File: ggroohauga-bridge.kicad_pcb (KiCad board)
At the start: 2 copper layers, 101.6 x 31 mm, 6 parts

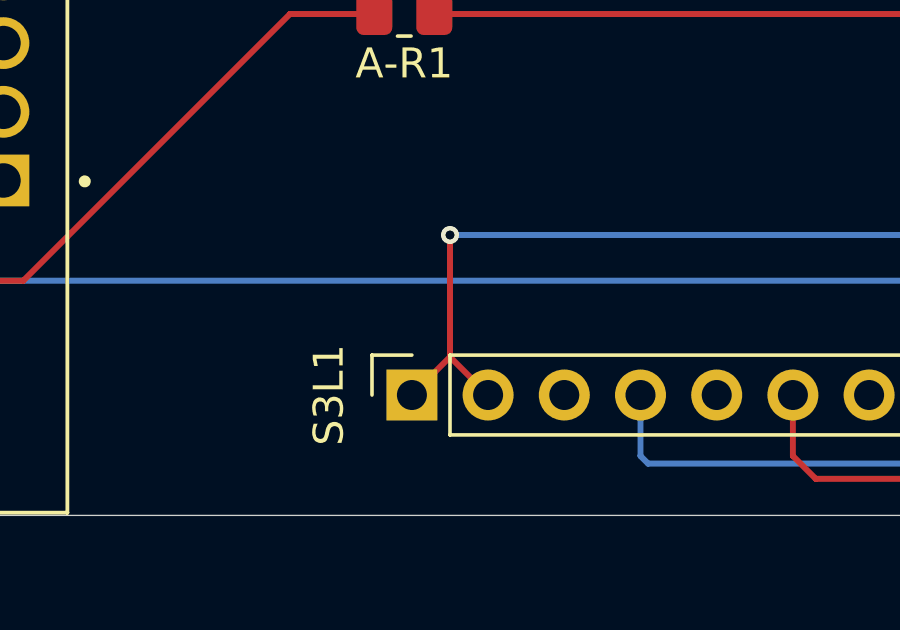
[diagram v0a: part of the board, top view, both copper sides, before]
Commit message: Fix compatibility with ESP32-S3-DevKitM-1
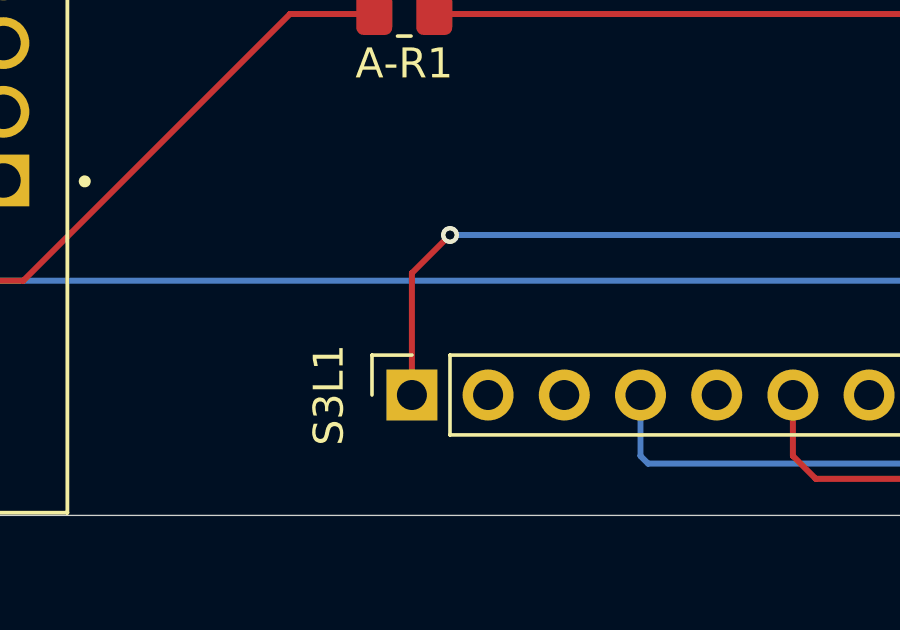
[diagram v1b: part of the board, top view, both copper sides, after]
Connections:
- S3L1 pad 2: +3.3V -> unconnected-(S3L1-Pin_2-Pad2)
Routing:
- net +3.3V: track 59.6 -> 57.8 mm
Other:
- board text added: "urn:oid:1.3.6.1.4.1.39777.1.3.1.3.1 https://github.com/nomis/ggroohauga-pcb (bridge)"
- board text removed: "urn:oid:1.3.6.1.4.1.39777.1.3.1.3.0 https://github.com/nomis/ggroohauga-pcb (bridge)"
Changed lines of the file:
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@@
 	(net 58 "unconnected-(C-J1-Pad3)")
 	(net 59 "unconnected-(C-J1-Pad4)")
+	(net 60 "unconnected-(S3L1-Pin_2-Pad2)")
 	(footprint "Connector_PinSocket_2.54mm:PinSocket_1x20_P2.54mm_Vertical"
 		(layer "F.Cu")
@@
 			)
 			(remove_unused_layers no)
-			(net 21 "+3.3V")
+			(net 60 "unconnected-(S3L1-Pin_2-Pad2)")
 			(pinfunction "Pin_2")
-			(pintype "passive")
+			(pintype "passive+no_connect")
 		)
 		(pad "3" thru_hole oval
@@
 		)
 	)
-	(gr_text "urn:oid:1.3.6.1.4.1.39777.1.3.1.3.0\nhttps://github.com/nomis/ggroohauga-pcb\n(bridge)\n"
+	(gr_text "urn:oid:1.3.6.1.4.1.39777.1.3.1.3.1\nhttps://github.com/nomis/ggroohauga-pcb\n(bridge)\n"
 		(at 131.064 66.04 0)
 		(layer "B.SilkS")
@@
 	)
 	(segment
-		(start 82.804 76.2)
-		(end 84.074 77.47)
+		(start 81.534 73.406)
+		(end 82.804 72.136)
 		(width 0.2)
 		(layer "F.Cu")
@@
 	(segment
 		(start 81.534 77.47)
-		(end 82.804 76.2)
-		(width 0.2)
-		(layer "F.Cu")
-		(net 21)
-	)
-	(segment
-		(start 82.804 72.136)
-		(end 82.804 76.2)
+		(end 81.534 73.406)
 		(width 0.2)
 		(layer "F.Cu")

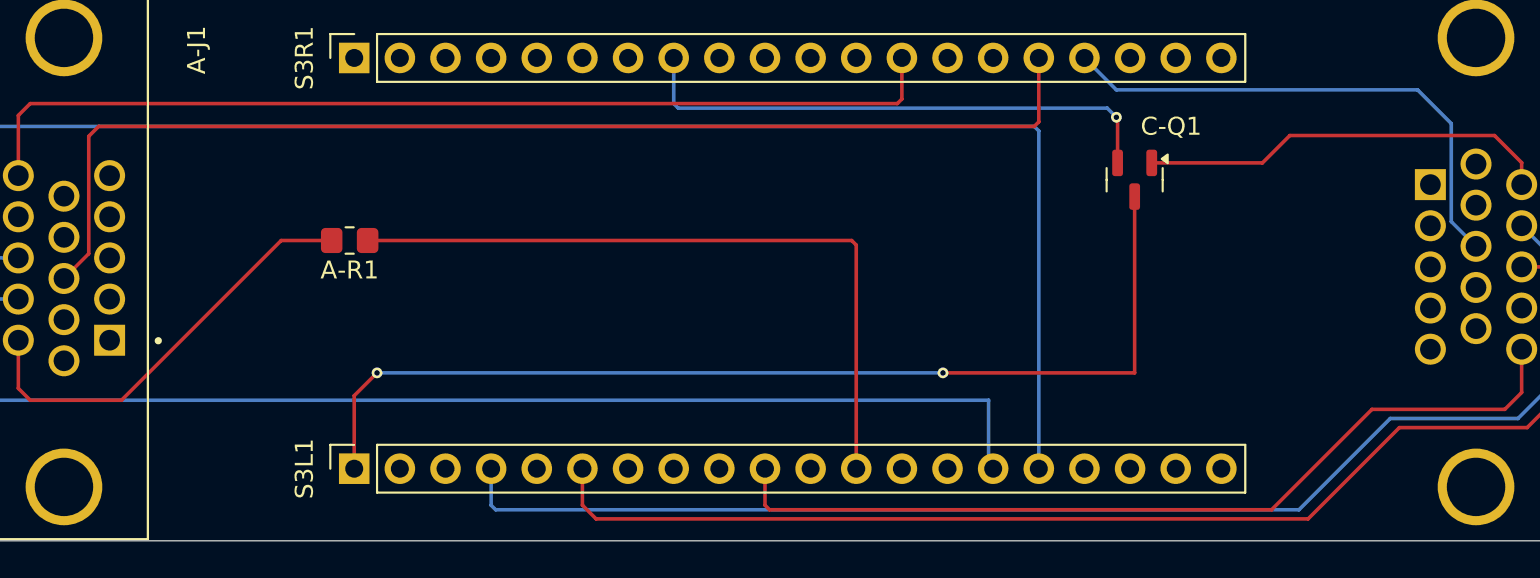
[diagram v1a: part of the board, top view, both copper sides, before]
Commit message: Connect audio pins on the bridge PCB
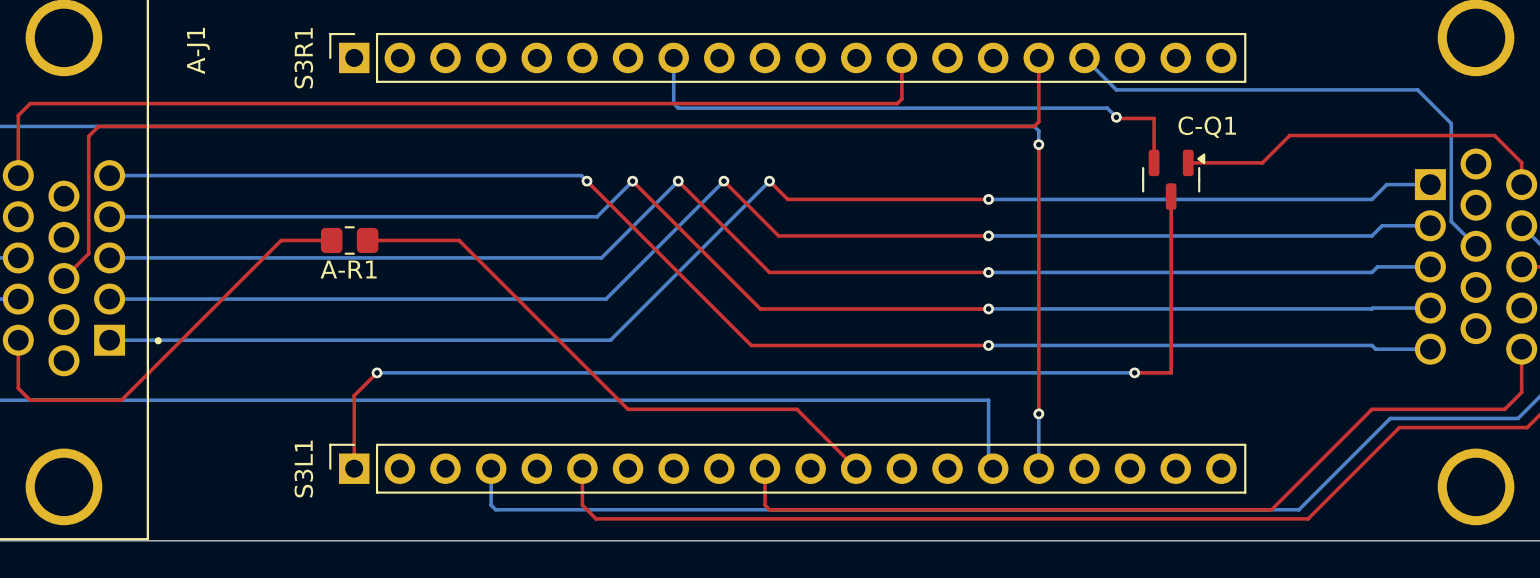
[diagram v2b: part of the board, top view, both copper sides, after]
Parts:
- moved C-Q1 2.03 mm to (127.0, 61.4)
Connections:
- A-J1 pad 1: unconnected-(A-J1-Pad1) -> AUDIO_HEADPHONES_R
- A-J1 pad 2: unconnected-(A-J1-Pad2) -> AUDIO_HEADPHONES_L
- A-J1 pad 3: unconnected-(A-J1-Pad3) -> AUDIO_GROUND
- A-J1 pad 4: unconnected-(A-J1-Pad4) -> AUDIO_AUX_R
- A-J1 pad 5: unconnected-(A-J1-Pad5) -> AUDIO_AUX_L
- A-J1 pad S1: GND -> (no net)
- A-J1 pad S2: GND -> (no net)
- C-J1 pad 1: unconnected-(C-J1-Pad1) -> AUDIO_HEADPHONES_R
- C-J1 pad 2: unconnected-(C-J1-Pad2) -> AUDIO_HEADPHONES_L
- C-J1 pad 3: unconnected-(C-J1-Pad3) -> AUDIO_GROUND
- C-J1 pad 4: unconnected-(C-J1-Pad4) -> AUDIO_AUX_R
- C-J1 pad 5: unconnected-(C-J1-Pad5) -> AUDIO_AUX_L
- C-J1 pad SH1: GND -> (no net)
- C-J1 pad SH2: GND -> (no net)
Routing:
- net AUDIO_HEADPHONES_R: track 0.00 -> 77.9 mm, vias 0 -> 2
- net AUDIO_HEADPHONES_L: track 0.00 -> 77.7 mm, vias 0 -> 2
- net AUDIO_GROUND: track 0.00 -> 77.5 mm, vias 0 -> 2
- net AUDIO_AUX_L: track 0.00 -> 77.5 mm, vias 0 -> 2
- net AUDIO_AUX_R: track 0.00 -> 77.3 mm, vias 0 -> 2
- net /GPIO_L8_C8_M10/AMP_POWER_IN: track 39.7 -> 32.5 mm
- net /CON_POWER_OUT: track 23.1 -> 21.0 mm
- net +3.3V: track 57.8 -> 59.9 mm
- net /GPIO_L40_C40_M41/CON_POWER_OUT: track 30.1 -> 32.1 mm
- net /GPIO_L10_C10_M14/AMP_RX: vias 0 -> 2

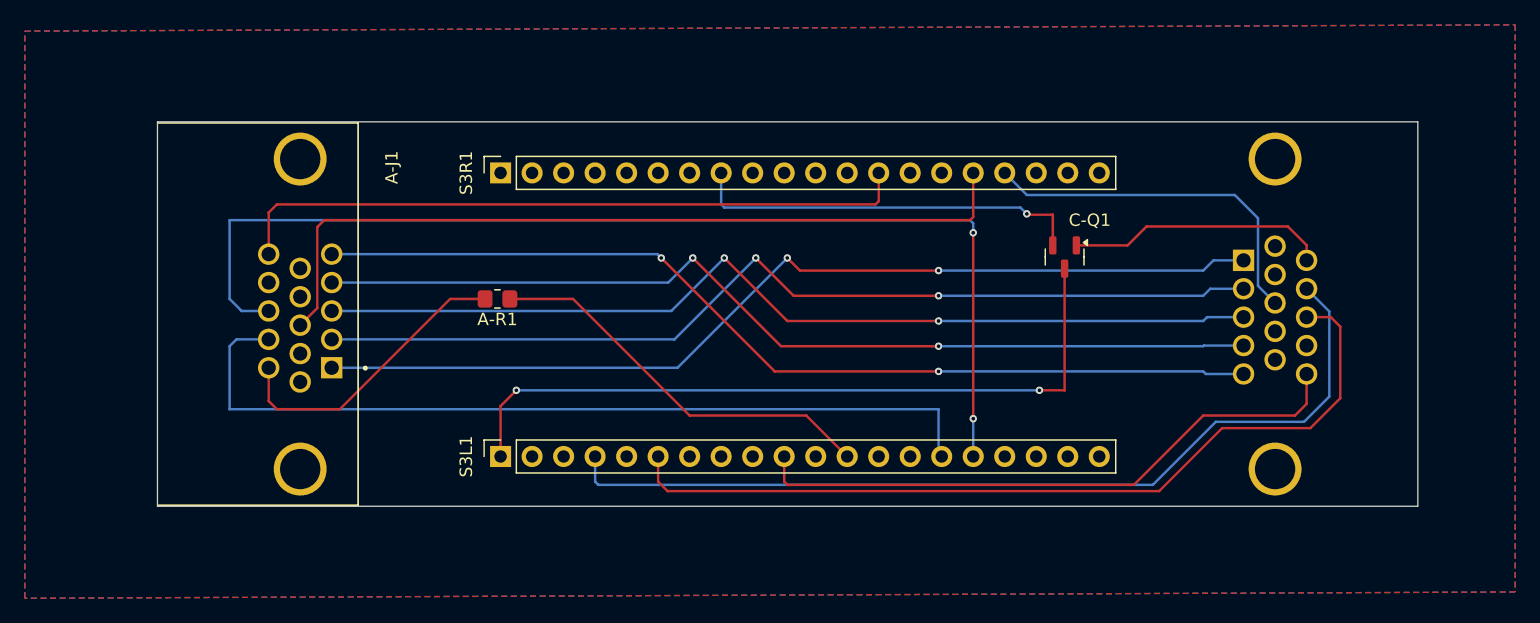
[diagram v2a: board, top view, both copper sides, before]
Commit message: Use thicker traces and vias for audio connections
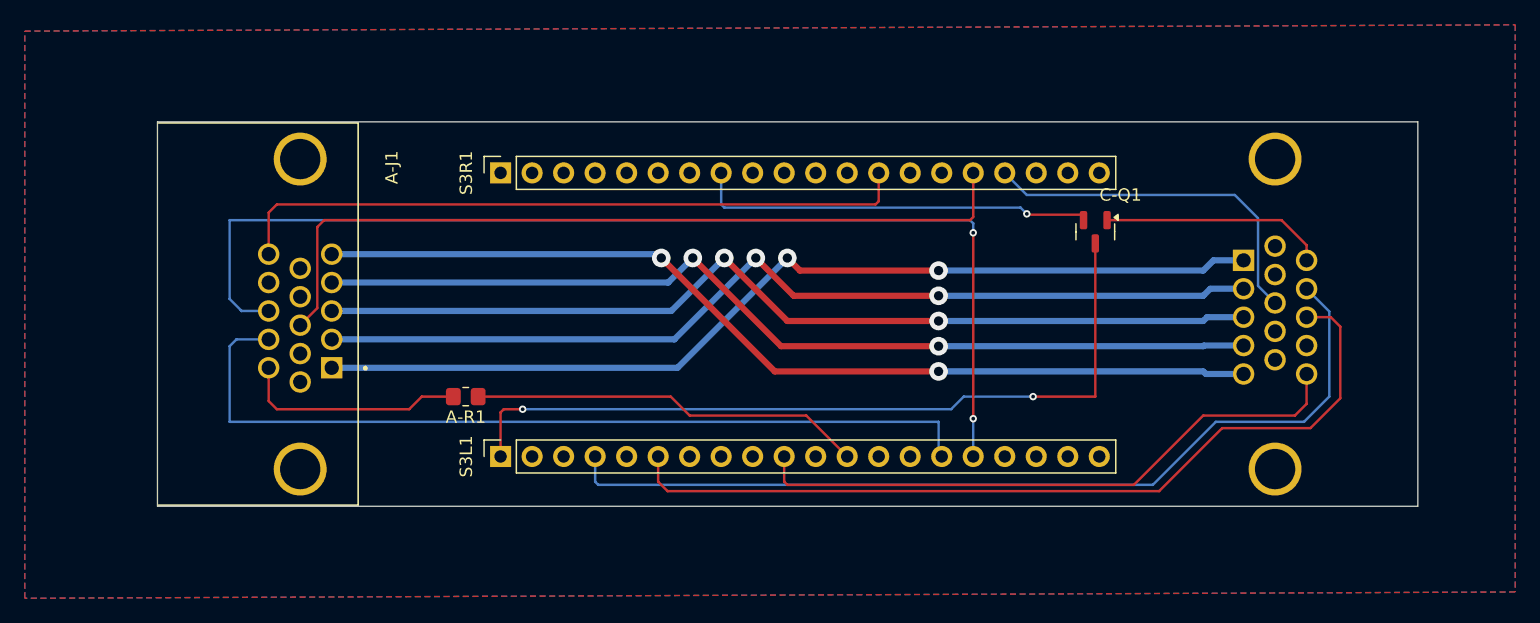
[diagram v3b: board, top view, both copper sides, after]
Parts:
- moved A-R1 8.28 mm to (78.7, 72.6)
- moved C-Q1 3.20 mm to (129.5, 59.4)
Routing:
- net /AMP_POWER_IN: track 24.1 -> 18.3 mm
- net +3.3V: track 59.9 -> 64.4 mm
- net /CON_POWER_OUT: track 21.0 -> 18.1 mm
- net /GPIO_L8_C8_M10/AMP_POWER_IN: track 32.5 -> 31.7 mm
